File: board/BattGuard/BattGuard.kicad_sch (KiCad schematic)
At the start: 158 parts, among them J1 OQ0271510000G, J10 Conn_01x01_Pin, J11 Conn_01x01_Pin, J12 Conn_01x01_Pin, J13 Conn_01x01_Pin, J14 Conn_01x01_Pin, J15 Conn_01x01_Pin, J17 S5B-XH-A, J18 FAN1 5V, J19 FAN2 5V, J2 Barrel_Jack, J3 Conn_01x22_Pin, J4 Conn_01x22_Pin, J5 Conn_01x02_Pin(xt60), J6 OLED DISPLAY, J7 EC5 JUMP CONNECTOR, J8 GSB4111312HR, J9 Conn_01x01_Pin, Q1 SIR680LDP-T1-RE3, Q2 SIR680LDP-T1-RE3, Q3 SIR680LDP-T1-RE3, Q4 SIR680LDP-T1-RE3, Q7 AO3401A, Q8 2N7002, Q9 AO3401A, SW1 SW_Push, SW2 SW_Push, U1 BQ25756ERRVR, U2 LMR51420XDDCR, U3 MCP45HV51-ST, U4 INA226, U5 LM317_TO3, U6 TLV76133KVUR, U7 TLV61047DDC

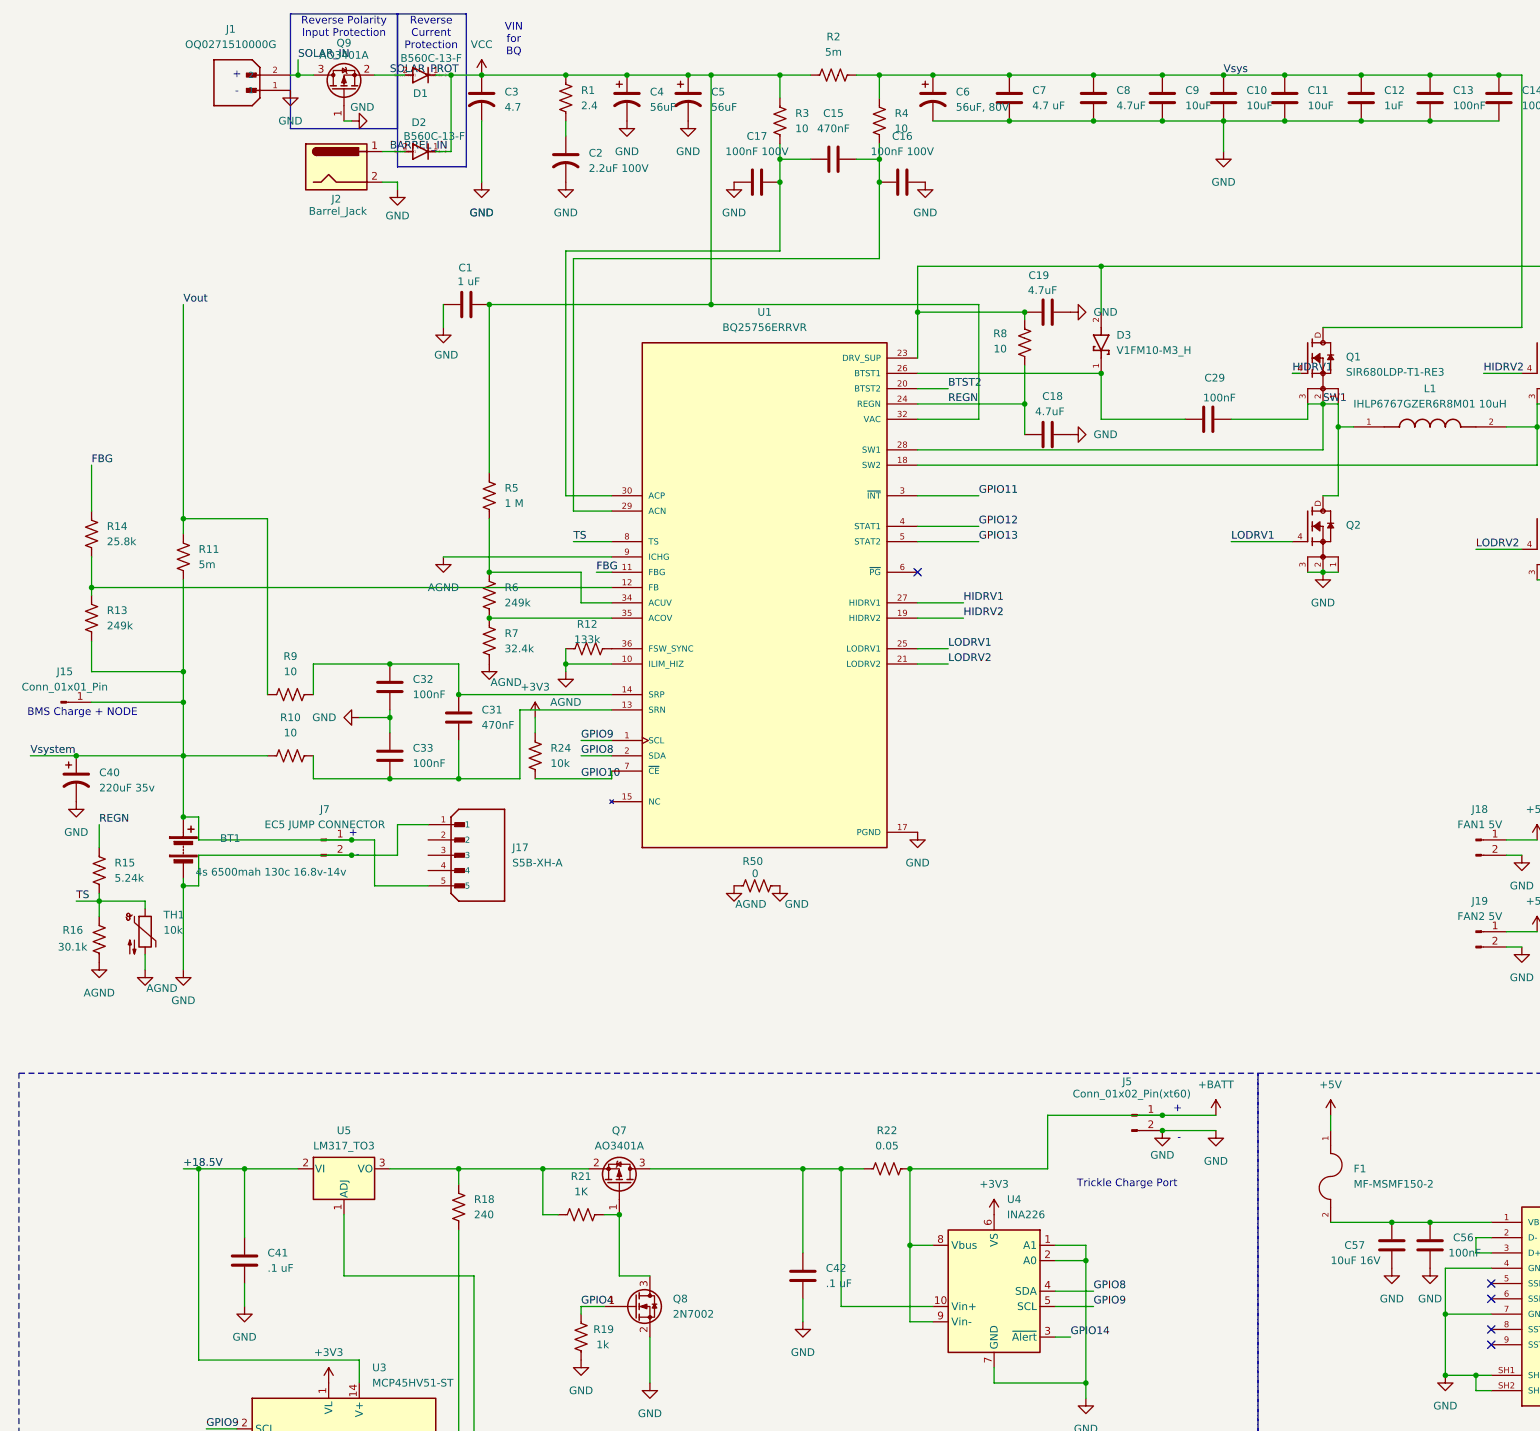
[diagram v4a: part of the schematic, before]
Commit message: ESD Protection Diodes + 60V 6.6A PMOS RV Prot
Updated schematic and layout to include 15V and 5V ESD protection diodes to the charge output. Also replaced undersized PMOS for solar reverse voltage input with 8-pin DIP DGS PMOSFET.
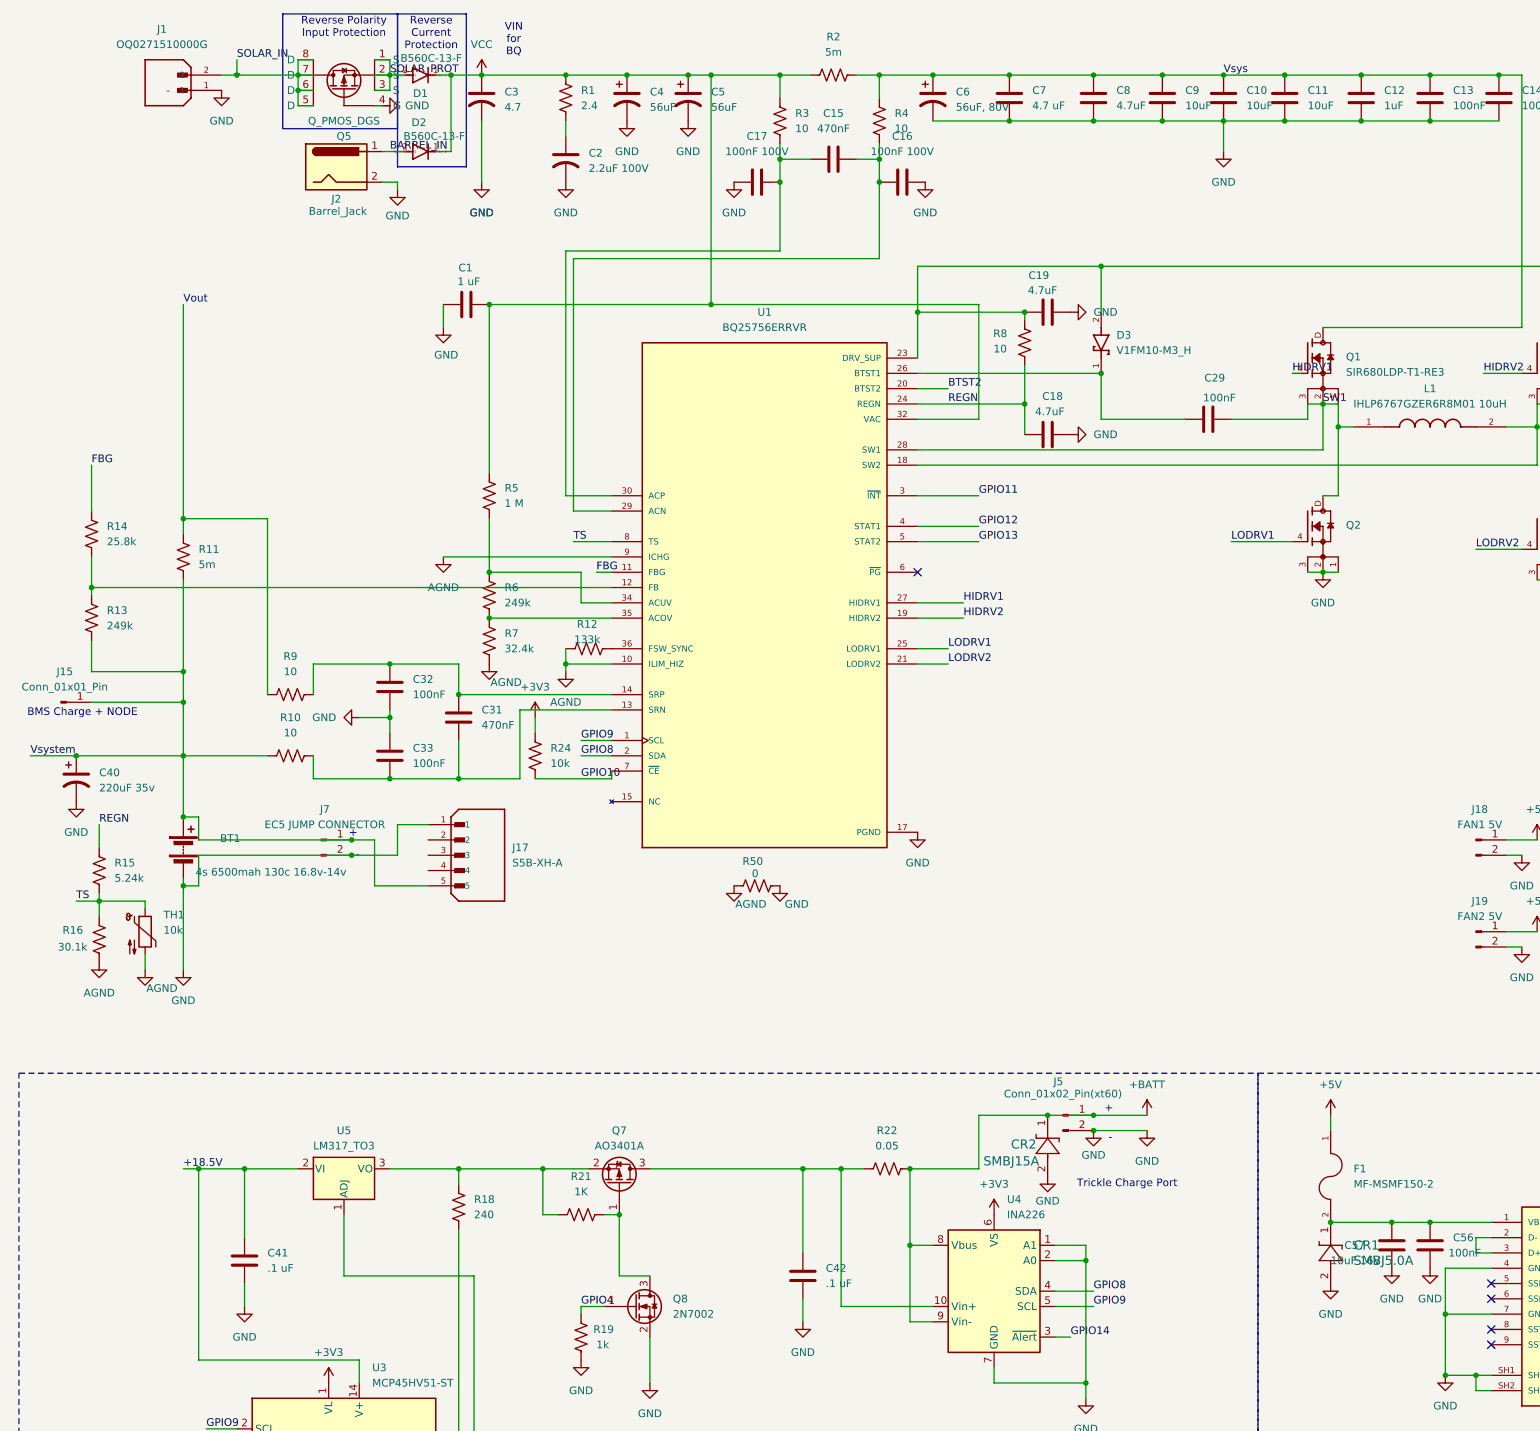
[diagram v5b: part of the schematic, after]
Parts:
- removed Q9: AO3401A, Package_TO_SOT_SMD:SOT-23, symbol Transistor_FET:AO3401A
- added CR1: SMBJ5.0A, DO-214AASMB_J-BEND_LTF, symbol TeamLib:SMBJ5.0A
- added CR2: SMBJ15A, DO-214AASMB_J-BEND_LTF, symbol TeamLib:SMBJ15A
- added Q5: Q_PMOS_DGS, TeamLib:SOIC127P600X175-8N, symbol TeamLib:DMP6023LSS-13
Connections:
- net +BATT: now also CR2.1
- net GND: now also CR1.2, CR2.2, Q5.4 (G)
- net SOLAR_IN: now also Q5.5 (D), Q5.6 (D), Q5.7 (D), Q5.8 (D)
- net SOLAR_PROT: now also Q5.1 (S), Q5.2 (S), Q5.3 (S)
- net at C56.1, C57.1, F1.2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: now also CR1.1
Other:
- moved on the sheet: J1, J5

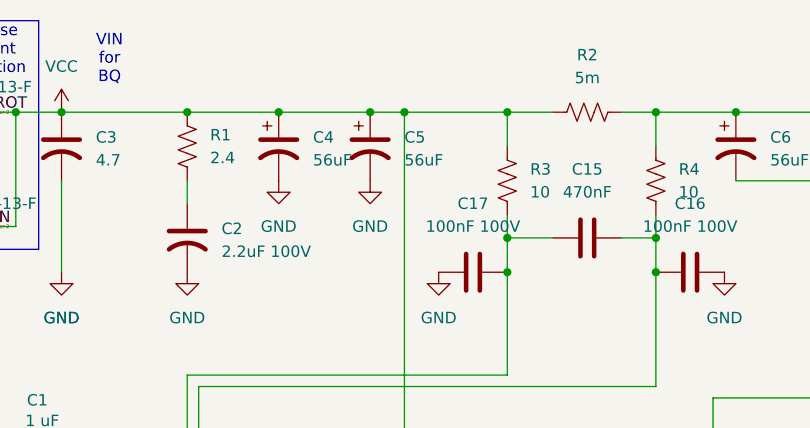
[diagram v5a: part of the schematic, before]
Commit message: 10.29.2026
Fixed pad connections around BQ, moved Thermisistor pads and setup vias for wires, keepout for inductor, placed oled header connector,
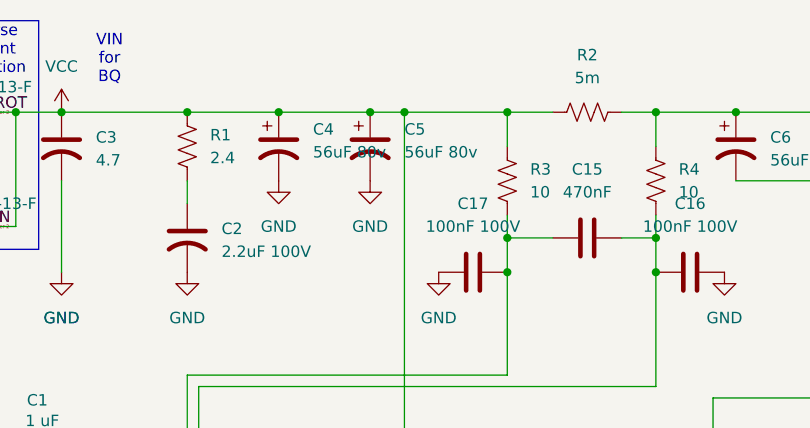
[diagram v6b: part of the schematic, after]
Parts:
- C4, C5: value 56uF -> 56uF 80v
- J6: footprint (none) -> Connector_PinHeader_2.54mm:PinHeader_1x05_P2.54mm_Vertical; now in the parts list
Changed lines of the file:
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@@
 		(fields_autoplaced yes)
 		(property "Reference" "C5"
-			(at 127 25.6539 0)
+			(at 127 24.7649 0)
 			(show_name no)
 			(do_not_autoplace no)
@@
 			)
 		)
-		(property "Value" "56uF"
-			(at 127 28.1939 0)
+		(property "Value" "56uF 80v"
+			(at 127 27.3049 0)
 			(show_name no)
 			(do_not_autoplace no)
@@
 		(body_style 1)
 		(exclude_from_sim no)
-		(in_bom no)
-		(on_board no)
+		(in_bom yes)
+		(on_board yes)
 		(in_pos_files yes)
 		(dnp no)
@@
 			)
 		)
-		(property "Footprint" ""
+		(property "Footprint" "Connector_PinHeader_2.54mm:PinHeader_1x05_P2.54mm_Vertical"
 			(at 334.01 133.35 0)
 			(hide yes)
@@
 		(fields_autoplaced yes)
 		(property "Reference" "C4"
-			(at 116.84 25.6539 0)
+			(at 116.84 24.7649 0)
 			(show_name no)
 			(do_not_autoplace no)
@@
 			)
 		)
-		(property "Value" "56uF"
-			(at 116.84 28.1939 0)
+		(property "Value" "56uF 80v"
+			(at 116.84 27.3049 0)
 			(show_name no)
 			(do_not_autoplace no)
